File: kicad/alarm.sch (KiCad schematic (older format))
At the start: 34 parts

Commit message: Finished rough schematic
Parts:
- removed U? (x2): 4027, symbol 4027
- added C4: 1u, symbol Device:CP1
- added R26, R36: 2k2, symbol Device:R
- added U17: 4027, symbol 4xxx_IEEE:4027
- added U19: NE555, symbol Timer:NE555
- C3, C5: renamed from C?; symbol C -> Device:C
- D1: renamed from D?; symbol D_Schottky_ALT -> Device:D_Schottky_ALT
- R16, R17, R18, R19, R20, R21, R22, R23, R24, R25, R27, R28, R29, R30, R31, R32, R33, R34, R35, R37: renamed from R?; symbol R -> Device:R
- SW1, SW4: renamed from SW?; symbol SW_DIP_x08 -> clock-rescue:SW_DIP_x08
- SW2, SW3: renamed from SW?; symbol SW_Push -> clock-rescue:SW_Push
- U15: renamed from U?; symbol 74LS390 -> clock-rescue:74LS390
- U16, U20: renamed from U?; symbol 74HC688 -> clock:74HC688
- U18: renamed from U?; symbol 74LS04 -> clock-rescue:74LS04
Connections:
- net labels added: 1Hz, BEEP, OFF
- wire segments 52 -> 103
- no-connect marks 2 -> 4
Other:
- note added: "Alarm Comparator, Sleep, and Beep"

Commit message: Fixed and prettied schematic
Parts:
- removed U15: 74HC390, symbol clock-rescue:74LS390
- removed U17: 4027, symbol 4xxx_IEEE:4027
- removed U18: 74LS04, symbol clock-rescue:74LS04
- added U1: 74HC04, symbol 74xx:74HC04
- added U15: 4027, symbol 4xxx:4027
- added U16: 74LS390, symbol 74xx:74LS390
- renumbered R16 to R21, R17 to R22, R18 to R23, R19 to R24, R20 to R25, R21 to R26, R22 to R27, R23 to R28, R24 to R29, R25 to R30, R26 to R31, R27 to R32, R28 to R33, R29 to R34, R30 to R35, R31 to R36, R32 to R37, R33 to R38, R34 to R39, R35 to R40, R36 to R41, R37 to R42, U16 to U17, U19 to U18, U20 to U19
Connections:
- net labels added: B0, B1, B2, B3, B4, B5, B6, B7, C0, C1, C2, C3, C4, C5, C6, C7, Q0, Q1, Q2, Q3, R0, R1, R2, R3, S0, S1, S2, S3, T0, T1, T2, T3
- wire segments 103 -> 184
- no-connect marks 4 -> 8
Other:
- moved on the sheet: R21, R22, R23, R24, R25, R26, R27, R28, SW1, SW4

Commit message: Some grouping
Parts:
- C3, C4, C5: footprint (none) -> Capacitors_THT:CP_Radial_D5.0mm_P2.00mm
- D1: footprint (none) -> Diodes_THT:D_A-405_P7.62mm_Horizontal
- R21, R22, R23, R24, R25, R26, R27, R28, R29, R30, R31, R32, R33, R34, R35, R36, R37, R38, R39, R40, R41, R42: footprint (none) -> Resistors_THT:R_Axial_DIN0207_L6.3mm_D2.5mm_P10.16mm_Horizontal
- SW1, SW4, U15, U16: footprint (none) -> Housings_DIP:DIP-16_W7.62mm
- SW2, SW3: footprint (none) -> Buttons_Switches_THT:SW_TH_Tactile_Omron_B3F-10xx
- U1: footprint (none) -> Housings_DIP:DIP-14_W7.62mm
- U17, U19: footprint (none) -> Housings_DIP:DIP-20_W7.62mm
- U18: footprint (none) -> Housings_DIP:DIP-8_W7.62mm
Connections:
- net Q0: now also U17.17 (A7); no longer U17.2 (A0)
- net Q1: now also U17.15 (A6); no longer U17.4 (A1)
- net Q2: now also U17.13 (A5); no longer U17.6 (A2)
- net Q3: now also U17.11 (A4); no longer U17.8 (A3)
- net R0: now also U17.8 (A3); no longer U17.11 (A4)
- net R1: now also U17.6 (A2); no longer U17.13 (A5)
- net R2: now also U17.4 (A1); no longer U17.15 (A6)
- net R3: now also U17.2 (A0); no longer U17.17 (A7)
- net S0: now also U19.17 (A7); no longer U19.2 (A0)
- net S1: now also U19.15 (A6); no longer U19.4 (A1)
- net S2: now also U19.13 (A5); no longer U19.6 (A2)
- net S3: now also U19.11 (A4); no longer U19.8 (A3)
- net T0: now also U19.8 (A3); no longer U19.11 (A4)
- net T1: now also U19.6 (A2); no longer U19.13 (A5)
- net T2: now also U19.4 (A1); no longer U19.15 (A6)
- net T3: now also U19.2 (A0); no longer U19.17 (A7)

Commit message: Fixed buses between sheets; comparator BCD inputs connected
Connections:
- net Q0 renamed ML0
- net Q1 renamed ML1
- net Q2 renamed ML2
- net Q3 renamed ML3
- net R0 renamed MH0
- net R1 renamed MH1
- net R2 renamed MH2
- net R3 renamed MH3
- net S0 renamed HL0
- net S1 renamed HL1
- net S2 renamed HL2
- net S3 renamed HL3
- net T0 renamed HH0
- net T1 renamed HH1
- net T2 renamed HH2
- net T3 renamed HH3
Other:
- moved on the sheet: C5, R21, R22, R23, R24, R25, R26, R27, R28, R32, R33, R34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

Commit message: More routing, but oops displays are backwards and it's all for nothing
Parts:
- renumbered R21 to R19, R22 to R20, R23 to R21, R24 to R22, R25 to R23, R26 to R24, R27 to R25, R28 to R26, R29 to R27, R30 to R28, R31 to R29, R40 to R30, R32 to R31, R33 to R32, R34 to R33, R35 to R34, R36 to R35, R37 to R36, R38 to R37, R39 to R38, R41 to R39, R42 to R40, U16 to U15, U15 to U16
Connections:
- no-connect marks 8 -> 9

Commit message: Routed switches
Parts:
- removed R31, R32, R33, R34, R35, R36, R37, R38: 22k, Resistors_THT:R_Axial_DIN0207_L6.3mm_D2.5mm_P10.16mm_Horizontal, symbol Device:R
- removed SW4: SW_DIP_x08, Housings_DIP:DIP-16_W7.62mm, symbol clock-rescue:SW_DIP_x08
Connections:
- net C0 is gone; now on net GND: U19.3 (B0)
- net C1 is gone; now on net GND: U19.5 (B1)
- net C2 is gone; now on net GND: U19.7 (B2)
- net C3 is gone; now on net GND: U19.9 (B3)
- net C4 is gone; now on net B0: U19.12 (B4)
- net C5 is gone; now on net B1: U19.14 (B5)
- net C6 is gone; now on net B2: U19.16 (B6)
- net C7 is gone; now on net B3: U19.18 (B7)
- net B0: no longer U17.3 (B0)
- net B1: no longer U17.5 (B1)
- net B2: no longer U17.7 (B2)
- net B3: no longer U17.9 (B3)
- net B4: now also U17.3 (B0); no longer U17.12 (B4)
- net B5: now also U17.5 (B1); no longer U17.14 (B5)
- net B6: now also U17.7 (B2); no longer U17.16 (B6)
- net B7: now also U17.9 (B3); no longer U17.18 (B7)
- net GND: now also U17.12 (B4), U17.14 (B5), U17.16 (B6), U17.18 (B7)

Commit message: Corrected schematic: SET button and discrete NAND blob
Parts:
- renumbered R24 to R10, R25 to R11, R26 to R12, R27 to R13, R28 to R14, R29 to R15, R30 to R16, R39 to R17, R40 to R18, R19 to R5, R20 to R6, R21 to R7, R22 to R8, R23 to R9, SW1 to SW2, SW2 to SW3, SW3 to SW4, U15 to U18, U16 to U19, U17 to U20, U18 to U21, U19 to U22

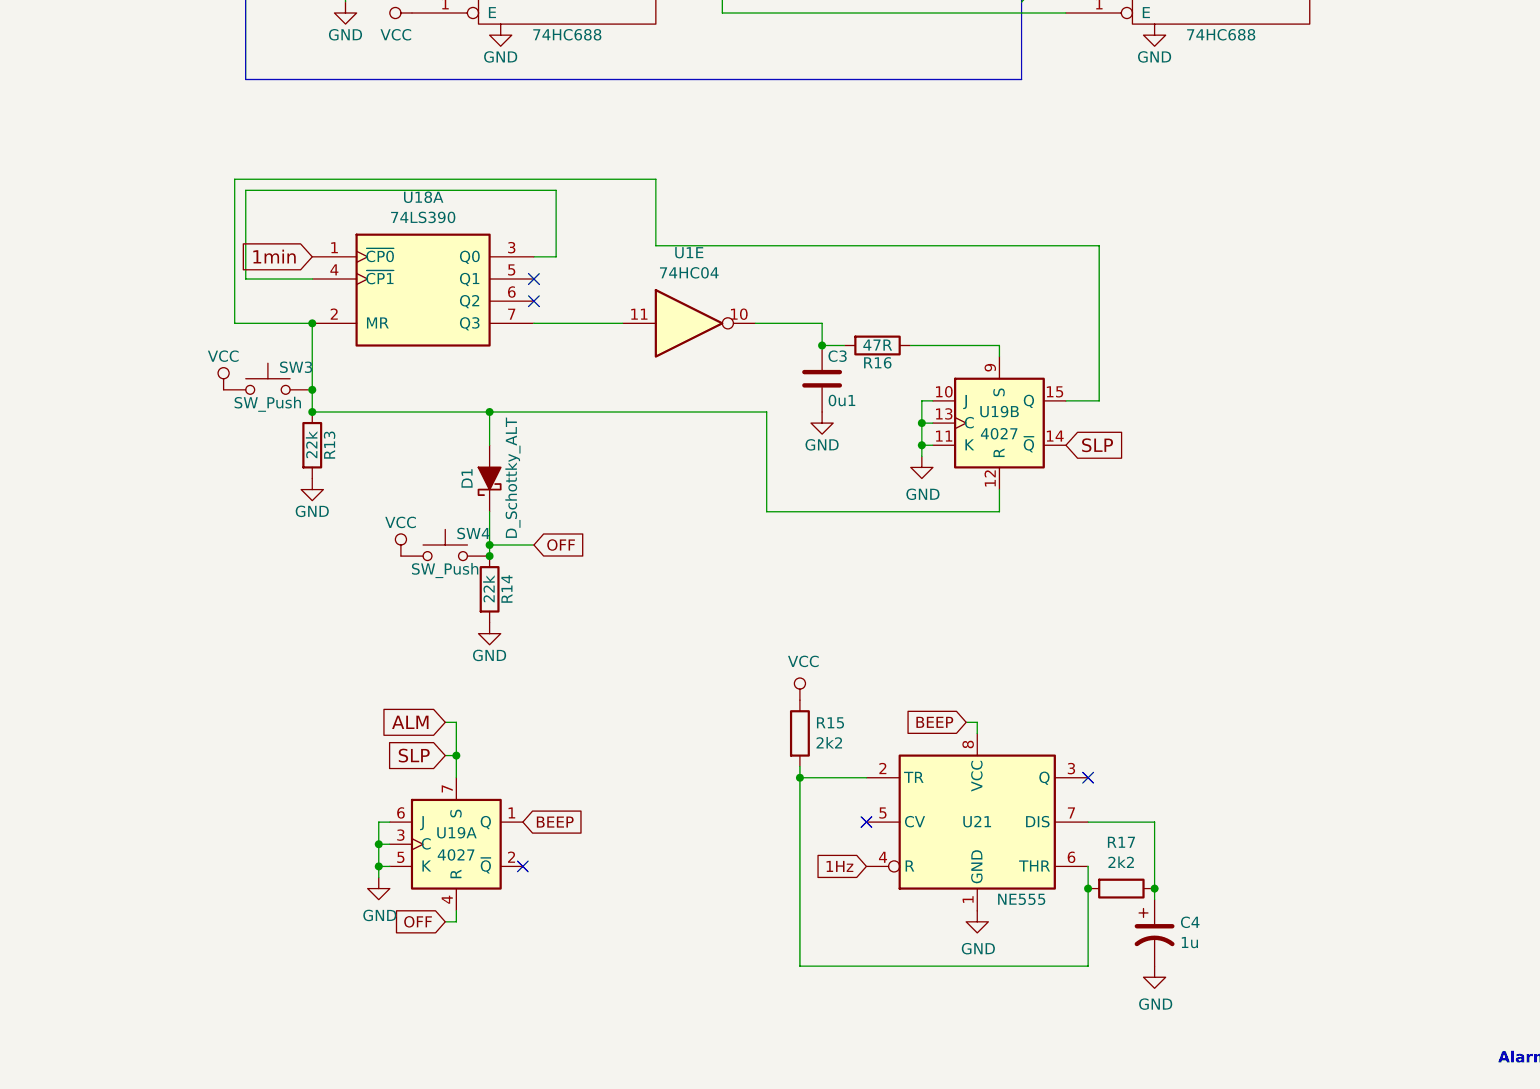
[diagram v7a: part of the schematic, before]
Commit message: New beeping circuit
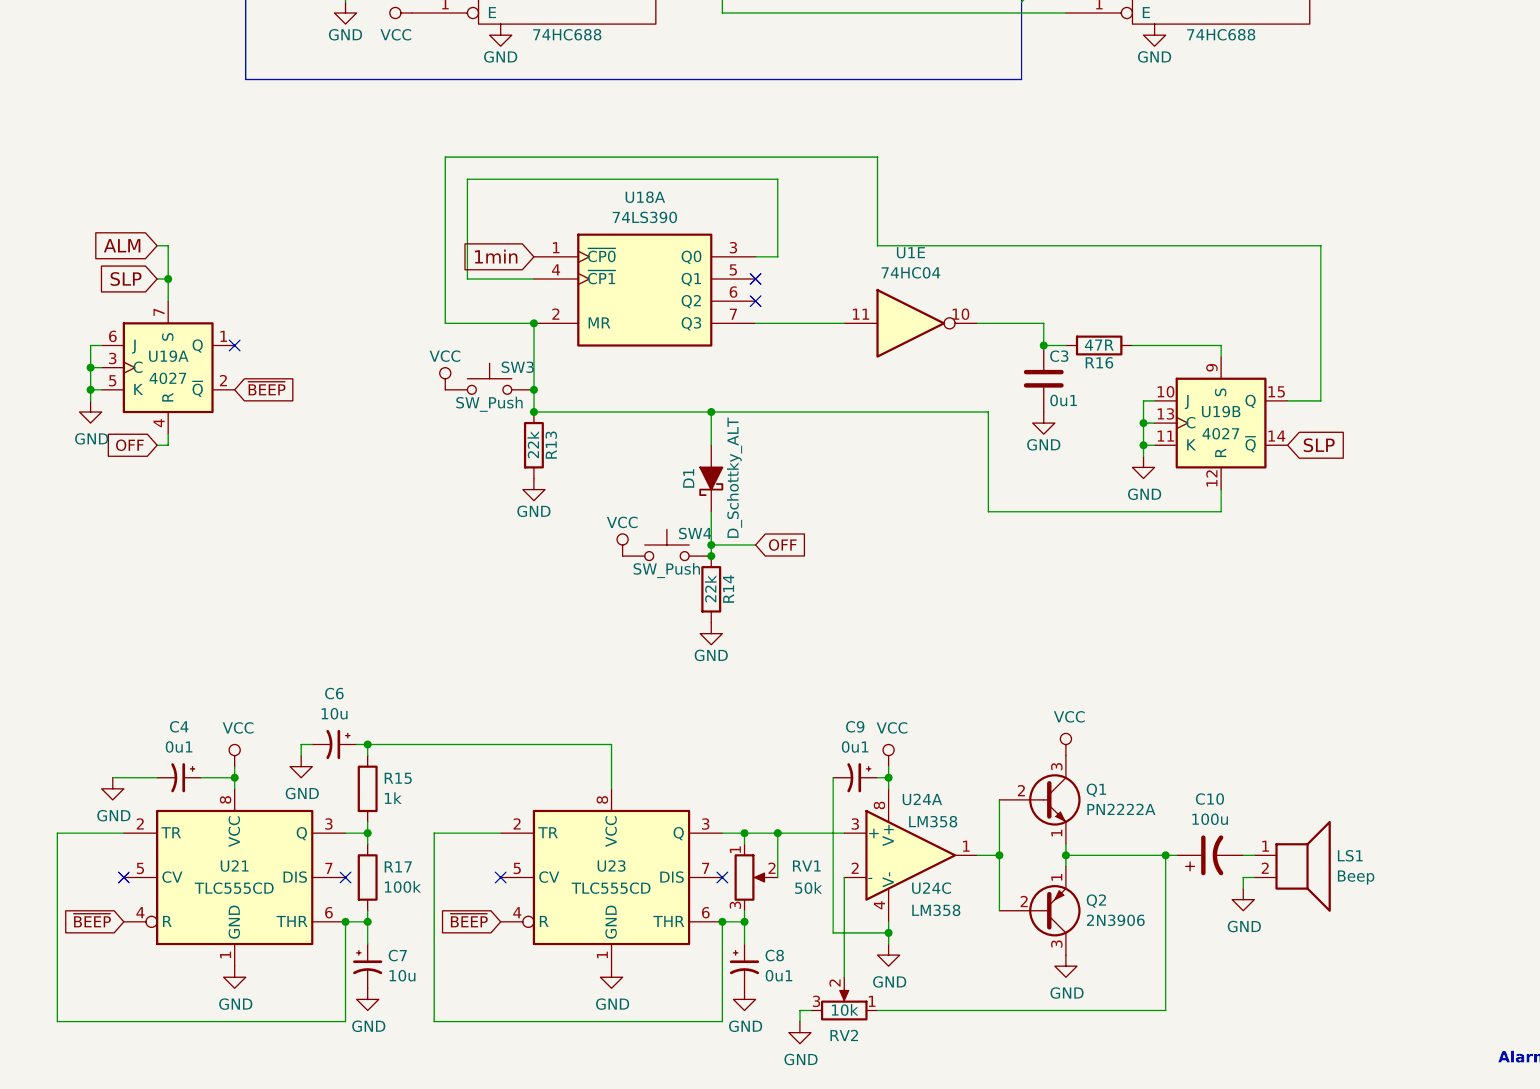
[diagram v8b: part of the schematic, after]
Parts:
- removed C4: 1u, Capacitors_THT:CP_Radial_D5.0mm_P2.00mm, symbol Device:CP1
- removed U21: NE555, Housings_DIP:DIP-8_W7.62mm, symbol Timer:NE555
- added C10: 100u, Capacitors_THT:CP_Radial_D7.5mm_P2.50mm, symbol Device:CP1
- added C4, C8, C9: 0u1, Capacitors_THT:CP_Radial_D5.0mm_P2.00mm, symbol Device:CP1_Small
- added C6, C7: 10u, Capacitors_THT:CP_Radial_D6.3mm_P2.50mm, symbol Device:CP1_Small
- added LS1: Beep, Wire_Connections_Bridges:WireConnection_1.00mmDrill, symbol Device:Speaker
- added Q1: PN2222A, TO_SOT_Packages_THT:TO-92_Inline_Narrow_Oval, symbol clock-rescue:PN2222A
- added Q2: 2N3906, TO_SOT_Packages_THT:TO-92_Inline_Narrow_Oval, symbol Transistor_BJT:2N3906
- added RV1: 50k, Potentiometers:Potentiometer_Trimmer_Bourns_3296W, symbol Device:R_POT
- added RV2: 10k, Potentiometers:Potentiometer_Trimmer_Bourns_3296W, symbol Device:R_POT
- added U21, U23: TLC555CD, Housings_SOIC:SOIC-8_3.9x4.9mm_Pitch1.27mm, symbol Timer:TLC555CD
- added U24: LM358, Housings_DIP:DIP-8_W7.62mm, symbol Amplifier_Operational:LM358
- R15: value 2k2 -> 1k
- R17: value 2k2 -> 100k
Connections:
- net GND: now also C4.2, C6.2, C7.2, C8.2, C9.2, LS1.2, Q2.3 (C), RV2.3, U21.1 (GND), U23.1 (GND), U24.4 (V-)
- net VCC: now also C4.1, C9.1, Q1.3 (C), U21.8 (VCC), U24.8 (V+); no longer R15.1
- net at R17.2: now also C7.1, U21.2 (TR), U21.6 (THR); no longer R15.2
- net at R17.1: now also R15.2, U21.3 (Q)
- net ~BEEP: now reaches U19.2 (~Q)
- net ~BEEP: now also U21.4 (R), U23.4 (R)
- net BEEP: no longer names the net of U19.1 (Q)
- new net: C8.1, RV1.3, U23.2 (TR), U23.6 (THR)
- new net: RV1.1, RV1.2, U23.3 (Q), U24.3 (+)
- new net: C6.1, R15.1, U23.8 (VCC)
- new net: Q1.2 (B), Q2.2 (B), U24.1
- new net: RV2.2, U24.2 (-)
- new net: C10.1, Q1.1 (E), Q2.1 (E), RV2.1
- new net: C10.2, LS1.1
- no-connect marks 9 -> 11
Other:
- moved on the sheet: C3, D1, R13, R14, R16, SW3, SW4, U18A, U19A, U19B, U1E
